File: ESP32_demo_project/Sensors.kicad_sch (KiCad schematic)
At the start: 18 parts, among them Q1 TEMT6000X01, U2 BME280, U7 MAX4466EXK

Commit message: main: updating layout
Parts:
- MK1: footprint CMC-5042PF-AC:CUI_CMC-5042PF-AC -> ESP32_project_Footprints:CUI_CMC-5042PF-AC
- Q1: footprint TEMT6000X01:TRANS_TEMT6000X01 -> ESP32_project_Footprints:TRANS_TEMT6000X01
- U2: footprint BME280:PSON65P250X250X100-8N -> ESP32_project_Footprints:PSON65P250X250X100-8N
- U7: footprint MAX4466EXK:SOT65P210X110-5N -> ESP32_project_Footprints:SOT65P210X110-5N
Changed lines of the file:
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@@
 			)
 		)
-		(property "Footprint" "BME280:PSON65P250X250X100-8N"
+		(property "Footprint" "ESP32_project_Footprints:PSON65P250X250X100-8N"
 			(at 67.31 50.8 0)
 			(effects
@@
 			)
 		)
-		(property "Footprint" "CMC-5042PF-AC:CUI_CMC-5042PF-AC"
+		(property "Footprint" "ESP32_project_Footprints:CUI_CMC-5042PF-AC"
 			(at 172.72 123.19 0)
 			(effects
@@
 			)
 		)
-		(property "Footprint" "TEMT6000X01:TRANS_TEMT6000X01"
+		(property "Footprint" "ESP32_project_Footprints:TRANS_TEMT6000X01"
 			(at 165.1 63.5 0)
 			(effects
@@
 			)
 		)
-		(property "Footprint" "MAX4466EXK:SOT65P210X110-5N"
+		(property "Footprint" "ESP32_project_Footprints:SOT65P210X110-5N"
 			(at 229.87 123.19 0)
 			(effects

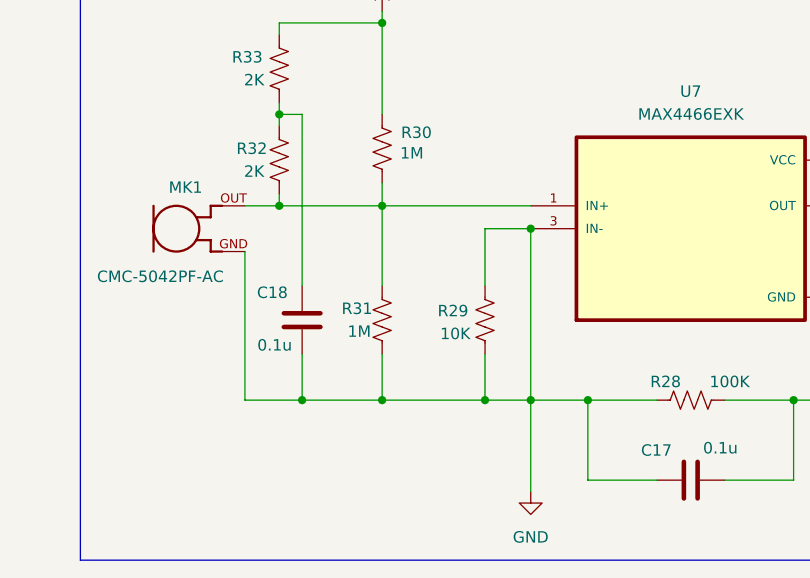
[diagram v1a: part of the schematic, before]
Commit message: main: updated placement
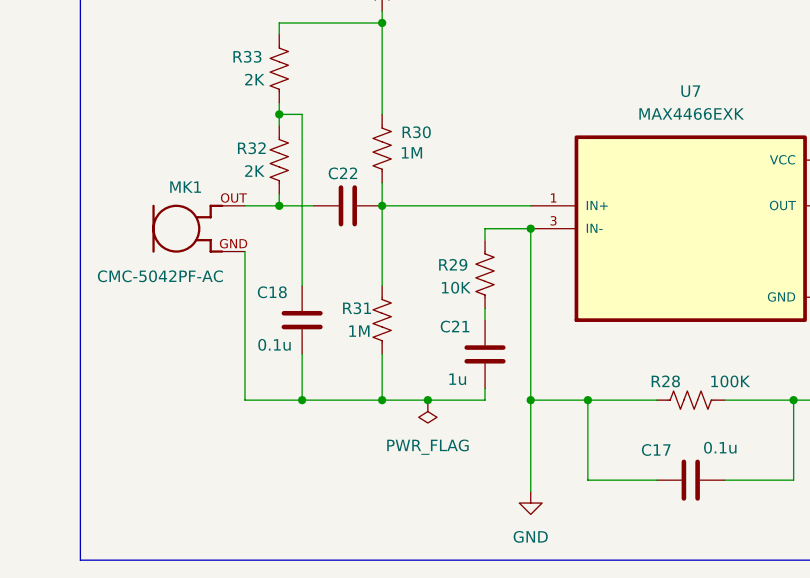
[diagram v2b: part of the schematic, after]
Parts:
- added C21: 1u, Capacitor_SMD:C_0805_2012Metric, symbol Device:C
- added C22: 1n, Capacitor_SMD:C_0805_2012Metric, symbol Device:C
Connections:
- net GND: no longer C18.2, MK1.GND, R29.1, R31.1
- net at R30.1, R31.2, U7.1 (IN+): now also C22.1; no longer MK1.OUT, R32.1
- new net: C18.2, C21.2, MK1.GND, R31.1
- new net: C22.2, MK1.OUT, R32.1
- new net: C21.1, R29.1
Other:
- moved on the sheet: R29
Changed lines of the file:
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@@
 	)
 	(junction
+		(at 200.66 142.24)
+		(diameter 0)
+		(color 0 0 0 0)
+	)
+	(junction
 		(at 41.91 30.48)
 		(diameter 0)
@@
 	)
 	(junction
-		(at 207.01 142.24)
-		(diameter 0)
-		(color 0 0 0 0)
-	)
-	(junction
 		(at 184.15 120.65)
 		(diameter 0)
@@
 	(wire
 		(pts
-			(xy 195.58 142.24) (xy 207.01 142.24)
+			(xy 195.58 142.24) (xy 200.66 142.24)
 		)
 		(stroke
@@
 	(wire
 		(pts
-			(xy 207.01 142.24) (xy 212.09 142.24)
-		)
-		(stroke
-			(width 0)
-			(type default)
-		)
-	)
-	(wire
-		(pts
 			(xy 218.44 151.13) (xy 218.44 142.24)
 		)
@@
 	(wire
 		(pts
-			(xy 207.01 123.19) (xy 207.01 129.54)
+			(xy 207.01 123.19) (xy 207.01 124.46)
 		)
 		(stroke
@@
 	(wire
 		(pts
+			(xy 207.01 140.97) (xy 207.01 142.24)
+		)
+		(stroke
+			(width 0)
+			(type default)
+		)
+	)
+	(wire
+		(pts
 			(xy 255.27 121.92) (xy 255.27 115.57)
 		)
@@
 	(wire
 		(pts
-			(xy 207.01 137.16) (xy 207.01 142.24)
+			(xy 200.66 142.24) (xy 207.01 142.24)
+		)
+		(stroke
+			(width 0)
+			(type default)
+		)
+	)
+	(wire
+		(pts
+			(xy 207.01 132.08) (xy 207.01 133.35)
 		)
 		(stroke
@@
 	(wire
 		(pts
-			(xy 184.15 120.65) (xy 195.58 120.65)
+			(xy 184.15 120.65) (xy 187.96 120.65)
 		)
 		(stroke
@@
 	)
 	(symbol
+		(lib_id "Device:C")
+		(at 207.01 137.16 0)
+		(mirror y)
+		(unit 1)
+		(exclude_from_sim no)
+		(in_bom yes)
+		(on_board yes)
+		(dnp no)
+		(property "Reference" "C21"
+			(at 203.708 134.112 0)
+			(effects
+				(font
+					(size 1.27 1.27)
+				)
+			)
+		)
+		(property "Value" "1u"
+			(at 203.962 139.954 0)
+			(effects
+				(font
+					(size 1.27 1.27)
+				)
+			)
+		)
+		(property "Footprint" "Capacitor_SMD:C_0805_2012Metric"
+			(at 206.0448 140.97 0)
+			(effects
+				(font
+					(size 1.27 1.27)
+				)
+				(hide yes)
+			)
+		)
+		(property "Datasheet" "~"
+			(at 207.01 137.16 0)
+			(effects
+				(font
+					(size 1.27 1.27)
+				)
+				(hide yes)
+			)
+		)
+		(property "Description" "Unpolarized capacitor"
+			(at 207.01 137.16 0)
+			(effects
+				(font
+					(size 1.27 1.27)
+				)
+				(hide yes)
+			)
+		)
+		(pin "2"
+		)
+		(pin "1"
+		)
+		(instances
+			(project "ESP32_demo_project"
+				(path "/bebedc1a-cede-44cf-af65-0ae0ecec96ba/261aef30-9265-4353-badb-9af4732a592d/e910f478-5103-4412-a008-27c86e3ebe47"
+					(reference "C21")
+					(unit 1)
+				)
+			)
+		)
+	)
+	(symbol
 		(lib_id "TEMT6000X01:TEMT6000X01")
 		(at 165.1 63.5 270)
@@
 	(symbol
 		(lib_id "Device:R_US")
-		(at 207.01 133.35 180)
+		(at 207.01 128.27 180)
 		(unit 1)
 		(exclude_from_sim no)
@@
 		(dnp no)
 		(property "Reference" "R29"
-			(at 203.454 132.334 0)
+			(at 203.454 127.254 0)
 			(effects
 				(font
@@
 		)
 		(property "Value" "10K"
-			(at 203.708 134.874 0)
+			(at 203.708 129.794 0)
 			(effects
 				(font
@@
 		)
 		(property "Footprint" "Resistor_SMD:R_0805_2012Metric"
-			(at 205.994 133.096 90)
+			(at 205.994 128.016 90)
 			(effects
 				(font
@@
 		)
 		(property "Datasheet" "~"
-			(at 207.01 133.35 0)
+			(at 207.01 128.27 0)
 			(effects
 				(font
@@
 		)
 		(property "Description" "Resistor, US symbol"
-			(at 207.01 133.35 0)
+			(at 207.01 128.27 0)
 			(effects
 				(font
@@
 	)
 	(symbol
+		(lib_id "power:PWR_FLAG")
+		(at 200.66 142.24 180)
+		(unit 1)
+		(exclude_from_sim no)
+		(in_bom yes)
+		(on_board yes)
+		(dnp no)
+		(fields_autoplaced yes)
+		(property "Reference" "#FLG05"
+			(at 200.66 144.145 0)
+			(effects
+				(font
+					(size 1.27 1.27)
+				)
+				(hide yes)
+			)
+		)
+		(property "Value" "PWR_FLAG"
+			(at 200.66 147.32 0)
+			(effects
+				(font
+					(size 1.27 1.27)
+				)
+			)
+		)
+		(property "Footprint" ""
+			(at 200.66 142.24 0)
+			(effects
+				(font
+					(size 1.27 1.27)
+				)
+				(hide yes)
+			)
+		)
+		(property "Datasheet" "~"
+			(at 200.66 142.24 0)
+			(effects
+				(font
+					(size 1.27 1.27)
+				)
+				(hide yes)
+			)
+		)
+		(property "Description" "Special symbol for telling ERC where power comes from"
+			(at 200.66 142.24 0)
+			(effects
+				(font
+					(size 1.27 1.27)
+				)
+				(hide yes)
+			)
+		)
+		(pin "1"
+		)
+		(instances
+			(project ""
+				(path "/bebedc1a-cede-44cf-af65-0ae0ecec96ba/261aef30-9265-4353-badb-9af4732a592d/e910f478-5103-4412-a008-27c86e3ebe47"
+					(reference "#FLG05")
+					(unit 1)
+				)
+			)
+		)
+	)
+	(symbol
 		(lib_id "MAX4466EXK:MAX4466EXK")
 		(at 229.87 123.19 0)
@@
 					(unit 1)
 				)
+			)
+		)
+	)
+	(symbol
+		(lib_id "Device:C")
+		(at 191.77 120.65 270)
+		(mirror x)
+		(unit 1)
+		(exclude_from_sim no)
+		(in_bom yes)
+		(on_board yes)
+		(dnp no)
+		(property "Reference" "C22"
+			(at 191.262 117.094 90)
+			(effects
+				(font
+					(size 1.27 1.27)
+				)
+			)
+		)
+		(property "Value" "1n"
+			(at 188.976 117.602 0)
+			(effects
+				(font
+					(size 1.27 1.27)
+				)
+				(hide yes)
+			)
+		)
+		(property "Footprint" "Capacitor_SMD:C_0805_2012Metric"
+			(at 187.96 119.6848 0)
+			(effects
+				(font
+					(size 1.27 1.27)
+				)
+				(hide yes)
+			)
+		)
+		(property "Datasheet" "~"
+			(at 191.77 120.65 0)
+			(effects
+				(font
+					(size 1.27 1.27)
+				)
+				(hide yes)
+			)
+		)
+		(property "Description" "Unpolarized capacitor"
+			(at 191.77 120.65 0)
+			(effects
+				(font
+					(size 1.27 1.27)
+				)
+				(hide yes)
+			)
+		)
+		(pin "2"
+		)
+		(pin "1"
+		)
+		(instances
+			(project "ESP32_demo_project"
+				(path "/bebedc1a-cede-44cf-af65-0ae0ecec96ba/261aef30-9265-4353-badb-9af4732a592d/e910f478-5103-4412-a008-27c86e3ebe47"
+					(reference "C22")
+					(unit 1)
+				)
